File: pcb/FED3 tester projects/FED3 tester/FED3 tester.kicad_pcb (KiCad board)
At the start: 4 copper layers, 108 x 82 mm, 156 parts, among them J1 USB4105-GF-A, J2 6pin_hd, J3 Conn_02x03_Odd_Even, J4 MotorCkeck, J5 Motor, J6 Conn_02x03_Odd_Even, J7 Conn_01x02_Socket, K1 1462042-8, K2 1462042-8, K3 1462042-8, Q1 DMN63D8L-7, Q2 DMN63D8L-7, Q3 DMN63D8L-7, Q4 DMN63D8L-7, SW1 SW_SPST, SW2 SW_SPST, SW3 SW_SPST, SW4 SW_SPST, SW5 SW_SPST, U1 FT232RL, U2 LP5907MFX-3.3, U3 TPS79301-EP, U4 THS4281, U5 THS4281, U6 THS4281, U7 THS4281, U8 ZXCT1082, U9 ATXMEGA32A4U-MH

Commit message: FED3 Tester - 1º routing finalizado
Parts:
- removed C36: 100nF, Capacitor_SMD:C_0402_1005Metric_Pad0.74x0.62mm_HandSolder
- removed the SW4 at (174.8, 111.0)
- removed the SW4 at (185.4, 111.3)
- added L2: 40R@100MHz, Resistor_SMD:R_0805_2012Metric, F.Cu at (133.8, 101.6)
- C1, C14, C15, C16, C17, C18, C19, C2, C20, C21, C22, C23, C24, C25, C26, C27, C28, C29, C3, C30, C31, C32, C33, C34, C35: footprint Capacitor_SMD:C_0402_1005Metric_Pad0.74x0.62mm_HandSolder -> Capacitor_SMD:C_0402_1005Metric
- R26, R27: footprint Resistor_SMD:R_0603_1608Metric -> Resistor_SMD:R_0402_1005Metric
- TP12, TP2, TP5, TP6, TP7, TP8: footprint FED3_PCBLib:Pin_D1.70mm -> FED3_PCBLib:Pin_D1.75mm
- moved R30 23.7 mm to (200.5, 55.4), turned to 0 degrees
- moved C17 15.5 mm to (174.0, 68.9), turned to 180 degrees
- moved R12 13.4 mm to (174.0, 70.5), turned to 0 degrees
- moved R26 12.6 mm to (186.0, 79.4)
- moved R44 12.0 mm to (145.2, 97.4), turned to -90 degrees
- moved C1 11.9 mm to (108.8, 86.5), turned to 180 degrees
- moved R29 11.6 mm to (157.6, 75.8), turned to 90 degrees
- moved D8 11.4 mm to (145.1, 90.8), turned to 90 degrees
- moved C16 11.0 mm to (174.0, 72.2), turned to 0 degrees
- moved C3 10.6 mm to (113.8, 95.6), turned to 0 degrees
- moved R28 10.5 mm to (159.5, 75.7), turned to -90 degrees
- moved R25 10.1 mm to (184.1, 80.5), turned to -90 degrees
- moved R27 10.1 mm to (186.0, 81.7), turned to 180 degrees
- moved R2 9.67 mm to (116.6, 95.6), turned to 0 degrees
- moved C14 9.36 mm to (170.7, 75.4), turned to 90 degrees
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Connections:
- D1 pad 1: USB+5V -> RELAY+5V
- D10 pad 1: USB+5V -> RELAY+5V
- D8 pad 1: USB+5V -> RELAY+5V
- K1 pad 8: USB+5V -> RELAY+5V
- K2 pad 8: USB+5V -> RELAY+5V
- K3 pad 8: USB+5V -> RELAY+5V
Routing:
- net +3V3: track 10.9 -> 539.8 mm, vias 0 -> 25
- net RELAY+5V: track 0.00 -> 144.0 mm, vias 0 -> 6
- net /main core/FTDI_CTS: track 0.00 -> 93.3 mm, vias 0 -> 3
- net Net-(R50-Pad2): track 0.00 -> 91.0 mm, vias 0 -> 2
- net /main core/FTDI_RXD: track 0.00 -> 89.9 mm, vias 0 -> 3
- net USB+5V: track 25.8 -> 115.0 mm, vias 0 -> 3
- net /main core/FTDI_RTS: track 0.00 -> 88.8 mm, vias 0 -> 3
- net /main core/FTDI_TXD: track 0.00 -> 86.3 mm, vias 0 -> 3
- net /main core/ADC Bat_I: track 0.00 -> 72.7 mm, vias 0 -> 2
- net /main core/LED_CHRG: track 0.00 -> 66.8 mm, vias 0 -> 1
- net Net-(R35-Pad2): track 0.00 -> 62.8 mm, vias 0 -> 2
- net /main core/STATE_LED: track 0.00 -> 62.0 mm, vias 0 -> 3
- net /main core/VUSB_check: track 1.90 -> 62.0 mm, vias 0 -> 3
- net Net-(R49-Pad2): track 0.00 -> 54.8 mm, vias 0 -> 1
- net /main core/Relay_ThermalPin: track 2.07 -> 56.3 mm, vias 0 -> 2
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- added copper zone on F.Cu, net +3V3

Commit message: FED3-tester
- 'final' - antes de revisão com o Filipe
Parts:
- removed R31, R32, R33, R34, R35: 100R, Resistor_SMD:R_0402_1005Metric
- C10: value 15pF -> 150pF
- J4: value MotorCkeck -> MotorCkeck1
- J5: value Motor -> MotorCkeck2
- K1, K2, K3: value 1462042-8 -> Relay SPDT
- R7: value 60k8 -> 61k2
- moved G*** 19.1 mm to (132.2, 41.3)
- moved K1 4.12 mm to (164.3, 90.1)
- moved D1 3.83 mm to (164.3, 82.7)
- moved D10 1.85 mm to (187.1, 61.5)
- moved K3 1.85 mm to (195.6, 61.4)
- moved R30 1.85 mm to (198.7, 55.4)
- moved C29 1.40 mm to (155.9, 60.2)
- moved Q4 1.20 mm to (189.8, 68.5)
- moved R47 1.20 mm to (186.1, 67.6)
- moved R48 1.20 mm to (186.1, 69.5)
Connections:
- SW1 pad 2: Net-(R31-Pad2) -> /main core/START_SW
- SW2 pad 2: Net-(R32-Pad2) -> /main core/Buzzer_OK
- SW3 pad 2: Net-(R33-Pad2) -> /main core/Buzzer_NOK
- SW4 pad 2: Net-(R34-Pad2) -> /main core/Motor_OK
- SW5 pad 2: Net-(R35-Pad2) -> /main core/Motor_NOK
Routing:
- net /main core/Motor_NOK: track 5.17 -> 68.7 mm, vias 0 -> 2
- net Net-(R35-Pad2): track 62.8 -> 0.00 mm, vias 2 -> 0
- net Net-(R34-Pad2): track 47.2 -> 0.00 mm, vias 2 -> 0
- net /main core/Motor_OK: track 5.71 -> 52.7 mm, vias 0 -> 2
- net /main core/Buzzer_NOK: track 8.28 -> 54.7 mm, vias 0 -> 2
- net Net-(R33-Pad2): track 45.6 -> 0.00 mm, vias 2 -> 0
- net /main core/START_SW: track 5.10 -> 44.8 mm, vias 0 -> 2
- net Net-(R31-Pad2): track 38.9 -> 0.00 mm, vias 2 -> 0
- net /main core/Buzzer_OK: track 6.86 -> 45.5 mm, vias 0 -> 2
- net Net-(R32-Pad2): track 37.6 -> 0.00 mm, vias 2 -> 0
- net GND: track 61.1 -> 94.0 mm, vias 38 -> 71
- net RELAY+5V: track 144.0 -> 136.8 mm
- net Net-(K1-Pad3): track 33.3 -> 37.3 mm
- net /main core/ADC Bat_I: track 72.7 -> 70.0 mm
- net Net-(R49-Pad2): track 54.8 -> 52.7 mm
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- added copper zone on B.Cu, net +3V3
- added copper zone on In1.Cu, net +3V3
- added copper zone on In2.Cu, net +3V3
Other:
- board text added: "LED CHRG"
- board text added: "POWER EN"
- board text added: "tester rev.A"
- board text removed: "FED3 tester rev.A"
- board text removed: "LED_CHRG"
- board text removed: "POWER_EN"

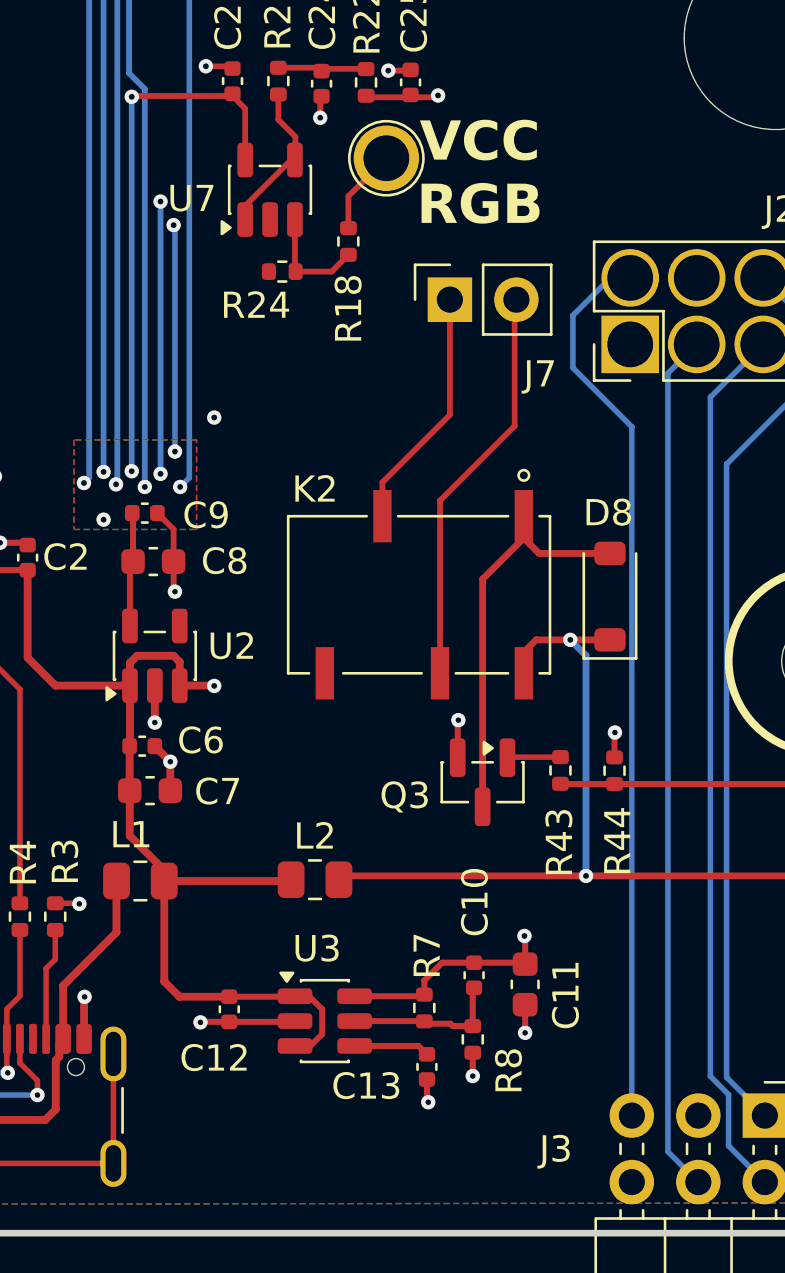
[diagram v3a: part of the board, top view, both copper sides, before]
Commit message: tunning com v.7.7
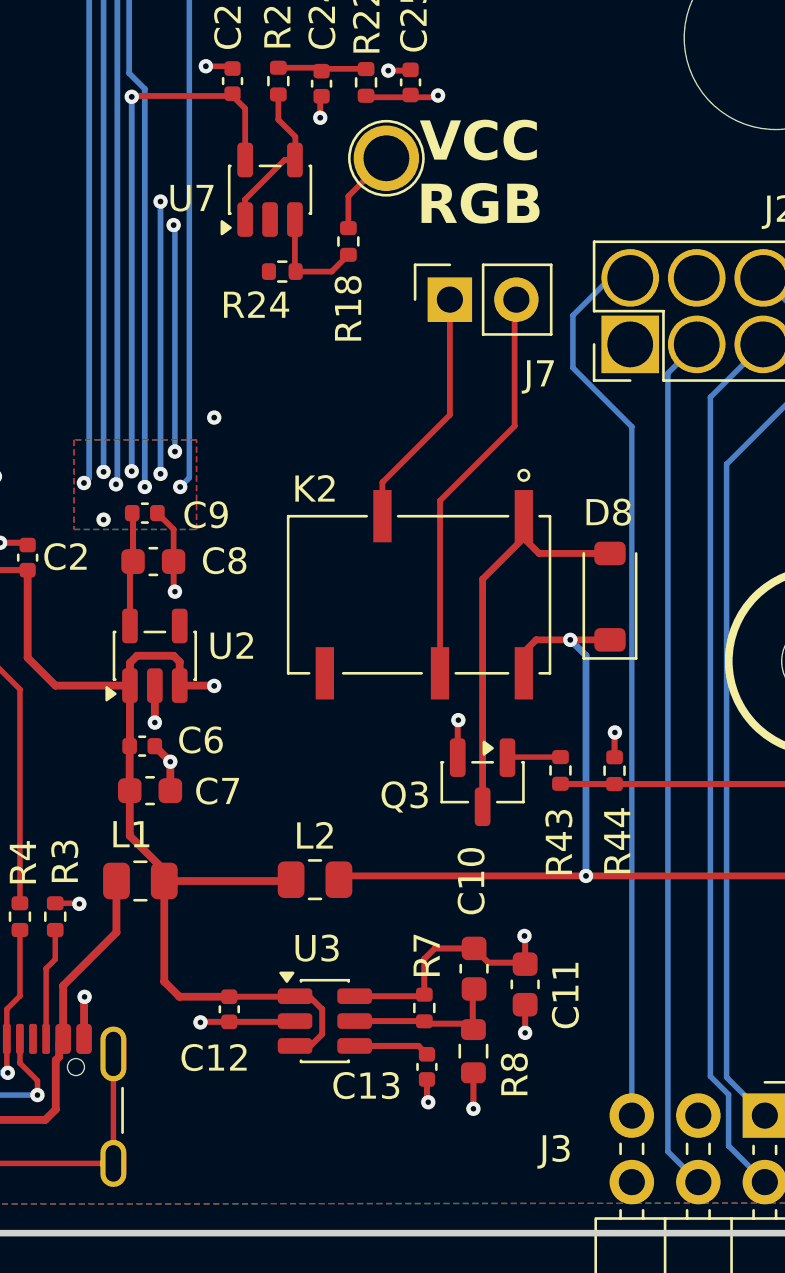
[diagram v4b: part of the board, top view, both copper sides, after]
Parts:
- C10: value 150pF -> 15pF; footprint Capacitor_SMD:C_0402_1005Metric -> Capacitor_SMD:C_0603_1608Metric
- R1, R15, R16, R23, R24, R3: value 5k1 -> 5.1k
- R26, R27: value 1k2 -> 1.2K
- R7: value 61k2 -> 61.2k
- R8: value 30k1 -> 30.1k; footprint Resistor_SMD:R_0402_1005Metric -> Resistor_SMD:R_0603_1608Metric
- U3: value TPS79301-EP -> TPS79301DBVRG4
- moved R8 0.45 mm to (139.8, 108.2)
- moved C10 0.25 mm to (139.9, 105.0)
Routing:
- net 3.7V: track 47.3 -> 48.2 mm
- net GND: track 94.0 -> 94.7 mm

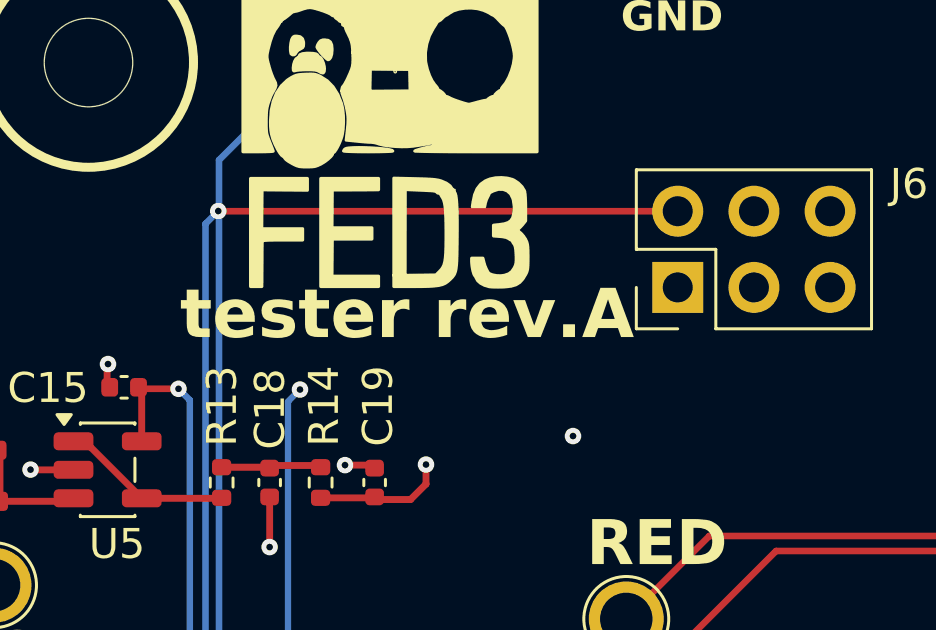
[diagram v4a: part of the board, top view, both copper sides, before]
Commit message: início FED3 tester - rev.B
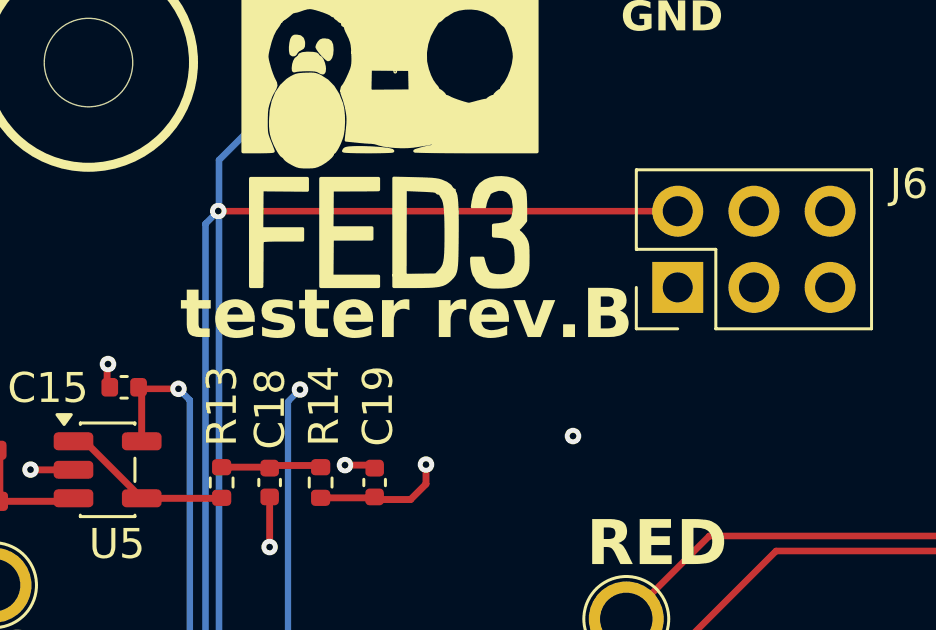
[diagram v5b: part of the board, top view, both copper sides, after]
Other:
- board text added: "tester rev.B"
- board text removed: "tester rev.A"
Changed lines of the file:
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@@
 		)
 	)
-	(gr_text "tester rev.A"
+	(gr_text "tester rev.B"
 		(at 125.4 49.8 0)
 		(layer "F.SilkS")

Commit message: FED3 tester project
.commit para sincronia
.ainda longe do final
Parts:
- removed the C20 at (112.2, 65.7)
- removed the C27 at (162.3, 50.7)
- removed the R19 at (115.0, 69.1)
- removed the R20 at (118.3, 69.1)
- removed the R23 at (107.1, 69.8)
- removed R49: 1k, Resistor_SMD:R_0402_1005Metric
- removed the TP11 at (120.0, 60.8)
- removed the U6 at (111.5, 68.6)
- added ?: , , F.Cu at (154.3, 183.4)
- added ?: , , F.Cu at (67.3, 183.5)
- added C10: 100nF, Capacitor_SMD:C_0402_1005Metric, F.Cu at (180.2, 17.0)
- added C11: 2.2uF, Capacitor_SMD:C_0603_1608Metric, F.Cu at (176.7, 17.3)
- added C12: 4.7uF, Capacitor_SMD:C_0603_1608Metric, F.Cu at (176.7, 19.8)
- added C13: 100nF, Capacitor_SMD:C_0402_1005Metric, F.Cu at (180.2, 19.0)
- added C24: 100nF, Capacitor_SMD:C_0402_1005Metric, F.Cu at (128.0, 143.7)
- added C25: 100nF, Capacitor_SMD:C_0402_1005Metric, F.Cu at (149.7, 144.4)
- added D5: Green, LED_SMD:LED_0603_1608Metric, F.Cu at (141.9, 116.8)
- added D8: Green, LED_SMD:LED_0603_1608Metric, F.Cu at (134.1, 182.9)
- added D9: Red, LED_SMD:LED_0603_1608Metric, F.Cu at (144.1, 182.8)
- added Q2: ???????, Package_TO_SOT_SMD:SOT-23, F.Cu at (75.6, 62.5)
- added Q3: DMN63D8L-7, Package_TO_SOT_SMD:SOT-23, F.Cu at (71.2, 62.5)
- added R13: 2k, Resistor_SMD:R_0402_1005Metric, F.Cu at (137.7, 116.8)
- added R18: 10k, Resistor_SMD:R_0402_1005Metric, F.Cu at (143.8, 176.7)
- added R27: 1.2K, Resistor_SMD:R_0402_1005Metric, F.Cu at (71.9, 58.6)
- added R29: 1.2K, Resistor_SMD:R_0402_1005Metric, F.Cu at (73.9, 58.6)
- added R32: 1.2K, Resistor_SMD:R_0402_1005Metric, F.Cu at (70.0, 58.6)
- added SW2: SW_SPST, Button_Switch_SMD:SW_SPST_TL3305B, F.Cu at (133.7, 101.2)
- added SW3: SW_SPST, Button_Switch_SMD:SW_SPST_TL3305B, F.Cu at (143.6, 101.2)
- added SW4: SW_SPST, Button_Switch_SMD:SW_SPST_TL3305B, F.Cu at (133.7, 144.8)
- added SW5: SW_SPST, Button_Switch_SMD:SW_SPST_TL3305B, F.Cu at (143.6, 144.8)
- added U3: LP5907MFX-3.3, Package_TO_SOT_SMD:SOT-23-5, F.Cu at (177.3, 13.8)
- C22, C23: value 15nF -> 100nF
- D1: renamed from D7; value Green LED -> Green
- D2: renamed from D6; value Green LED -> Green
- D3: renamed from D5; value Green LED -> Green
- D4: value Green LED -> Green
- D7: renamed from D3; value Green LED -> Red
- R10: renamed from R41; value 330R -> 2k
- R11: renamed from R40; value 330R -> 2k
- R12: renamed from R39; value 330R -> 2k
- R15: renamed from R38; value 330R -> 10k
- R17: value 10k -> 2k
- R9: renamed from R42; value 560R -> 2k
- moved R17 111.4 mm to (134.4, 176.3)
- moved C29 103.9 mm to (128.4, 162.4)
- moved C30 98.6 mm to (149.6, 162.5)
- moved J1 83.5 mm to (81.5, 184.5)
- moved J4 81.5 mm to (110.7, 181.4)
- moved SW9 78.5 mm to (143.6, 163.4)
- moved SW8 77.7 mm to (133.7, 163.4)
- moved C27 75.5 mm to (127.8, 125.1), turned to -90 degrees
- moved C28 67.2 mm to (150.2, 125.8), turned to -90 degrees
- moved SW7 47.7 mm to (143.6, 126.1)
- moved SW6 46.6 mm to (133.7, 126.1)
- moved C23 43.5 mm to (150.6, 100.0), turned to -90 degrees
- moved SW1 42.1 mm to (139.1, 80.5)
- moved ? 41.2 mm to (111.1, 60.6)
- moved C38 41.2 mm to (93.8, 62.3)
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- renumbered C10 to C14, C11 to C15, C12 to C16, C13 to C17, C26 to C18, C28 to C19, C29 to C20, C30 to C21, C35 to C26, C33 to C27, C34 to C28, C31 to C29, C32 to C30, C14 to C31, C15 to C32, C16 to C33, C17 to C34, C18 to C35, C19 to C36, C21 to C37, C24 to C38, C25 to C39, D1 to D10, D8 to D11, D10 to D12, D2 to D6, J6 to J2, J2 to J3, J3 to J4, J4 to J5, J5 to J6, Q2 to Q1, Q1 to Q4, Q3 to Q5, Q4 to Q6, R36 to R14, R37 to R16, R9 to R19, R10 to R20, R11 to R21, R12 to R22, R13 to R23, R14 to R24, R15 to R25, R16 to R26, R18 to R28, R21 to R30, R22 to R31, R24 to R33, R25 to R34, R50 to R35, R45 to R36, R26 to R37, R27 to R38, R28 to R39, R43 to R40, R29 to R41, R44 to R42, R46 to R43, R30 to R44, R47 to R45, R48 to R46, SW4 to SW6, SW5 to SW7, SW2 to SW8, SW3 to SW9, TP12 to TP11, TP13 to TP12, TP7 to TP4, TP8 to TP5, TP5 to TP6, TP6 to TP7, TP4 to TP8, U3 to U4, U9 to U5, U4 to U6, U5 to U7, U7 to U8, U8 to U9
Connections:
- net /main core/DUT stage/SWCLK renamed /main core/DUT stage/DUT_SWCLK
- net /main core/DUT stage/SWDIO renamed /main core/DUT stage/DUT_SWDIO
- net /main core/DUT stage/~{RESET} renamed /main core/DUT stage/DUT_~{RESET}
- C22 pad 1: Net-(C22-Pad1) -> /main core/Prog_OK
- C23 pad 1: /main core/VUSB_check -> /main core/Prog_NOK
- R10 pad 2: /main core/LED#3 -> /main core/LED#2
- R11 pad 2: /main core/LED#2 -> /main core/LED#3
- R12 pad 2: /main core/LED#1 -> /main core/LED#4
- R17 pad 2: /main core/DUT stage/VUSBtest -> /main core/PASS
- R9 pad 2: /main core/LED#4 -> /main core/LED#1
- TP8 pad 1: /main core/DUT stage/VUSBtest -> /main core/DUT stage/VUSB_out
- U5 pad 14: unconnected-(U9-PC4/OC1A/~{SS}-Pad14) -> /main core/LED#5
- U5 pad 15: unconnected-(U9-PC5/OC1B/MOSI/XCK1-Pad15) -> /main core/PASS
- U5 pad 16: unconnected-(U9-PC6/MISO/RXD1-Pad16) -> /main core/FAIL
- U5 pad 21: /main core/Buzzer_OK -> /main core/Prog_OK
- U5 pad 22: /main core/Buzzer_NOK -> /main core/Prog_NOK
- U5 pad 23: /main core/Motor_OK -> /main core/RGBW_OK
- U5 pad 24: /main core/Motor_NOK -> /main core/RGBW_NOK
- U5 pad 25: unconnected-(U9-PD5/OC1B/XCK1/MOSI-Pad25) -> /main core/Motor_OK
- U5 pad 26: /main core/~{RESET}_Test -> /main core/Motor_NOK
- U5 pad 27: /main core/POWER_EN -> /main core/Buzzer_OK
- U5 pad 39: +3V3 -> AVCC
- U5 pad 40: /main core/VBattest_check -> /main core/Buzzer_NOK
- U5 pad 41: /main core/VUSB_check -> /main core/VBattest_check
- U5 pad 42: /main core/VccRGB_check -> /main core/VUSB_2DUT
- U5 pad 6: unconnected-(U9-PB2/ADC10/DAC0-Pad6) -> /main core/I ON/OFF Test
- U5 pad 7: /main core/I ON/OFF Test -> /main core/POWER_EN
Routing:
- net /main core/Motor_NOK: track 68.7 -> 4.18 mm, vias 2 -> 0
- net /main core/VUSB_check: track 61.7 -> 0.00 mm, vias 3 -> 0
- net /main core/VBattest_check: track 34.8 -> 93.7 mm, vias 3 -> 5
- net /main core/Buzzer_NOK: track 54.7 -> 0.00 mm, vias 2 -> 0
- net /main core/Motor_OK: track 52.7 -> 0.00 mm, vias 2 -> 0
- net Net-(R49-Pad2): track 52.7 -> 0.00 mm, vias 1 -> 0
- net (no net): track 0.00 -> 52.7 mm, vias 0 -> 1
- net /main core/Buzzer_OK: track 45.5 -> 0.00 mm, vias 2 -> 0
- net /main core/Prog_NOK: track 0.00 -> 37.9 mm, vias 0 -> 2
- net /main core/Prog_OK: track 0.00 -> 36.3 mm, vias 0 -> 2
- net GND: track 94.7 -> 70.5 mm, vias 71 -> 55
- net /main core/RGBW_NOK: track 0.00 -> 19.8 mm, vias 0 -> 1
- net RELAY+5V: track 136.8 -> 118.4 mm
- net /main core/RGBW_OK: track 0.00 -> 16.1 mm, vias 0 -> 1
- net Net-(U6--) (its old number): track 4.97 -> 0.00 mm
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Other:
- board size 108 x 82 mm -> 108 x 164 mm
- board text added: "FINAL RESULT"
- board text added: "all rgbw ok?"
- board text added: "buzzer ok?"
- board text added: "motor moved left & right?"
- board text added: "programming ok?"
- board text removed: "STEP 1"
- board text removed: "STEP 2"

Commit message: FED3 tester - sync of the week
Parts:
- removed C14: 15pF, Capacitor_SMD:C_0603_1608Metric
- removed the C17 at (97.8, 99.9)
- added R39: 640k, Resistor_SMD:R_0402_1005Metric, F.Cu at (60.7, 39.3)
- added R42: 1M, Resistor_SMD:R_0402_1005Metric, F.Cu at (60.7, 41.3)
- C15: value 4.7uF -> 10uF; footprint Capacitor_SMD:C_0603_1608Metric -> Capacitor_SMD:C_1206_3216Metric
- R29: value 1.2K -> 1.2K ??
- R7: value 61.2k -> 8k2
- R8: value 30.1k -> 4k; footprint Resistor_SMD:R_0603_1608Metric -> Resistor_SMD:R_0402_1005Metric
- U4: value TPS79301DBVRG4 -> TPS73801DCQR; footprint Package_TO_SOT_SMD:SOT-23-6 -> Package_TO_SOT_SMD:SOT-223-6
- moved D7 62.3 mm to (54.3, 86.6), turned to -90 degrees
- moved C2 62.0 mm to (85.2, 142.4), turned to 0 degrees
- moved R15 59.0 mm to (56.8, 86.9)
- moved U1 56.4 mm to (85.7, 135.4), turned to -90 degrees
- moved C1 54.4 mm to (88.0, 128.4), turned to 90 degrees
- moved C5 52.5 mm to (76.4, 147.5)
- moved R1 52.5 mm to (79.6, 146.6)
- moved R3 52.5 mm to (83.6, 146.6)
- moved R4 52.5 mm to (82.3, 146.6)
- moved R5 52.5 mm to (80.9, 146.6)
- moved C4 52.5 mm to (76.4, 149.0)
- moved R6 52.5 mm to (76.4, 146.2)
- moved R2 49.5 mm to (78.9, 136.2), turned to -90 degrees
- moved C3 47.0 mm to (78.9, 133.4), turned to -90 degrees
- moved L1 44.3 mm to (74.3, 135.3), turned to 90 degrees
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- renumbered C18 to C17, C19 to C18, C20 to C19, C21 to C20, C22 to C21, C23 to C22, C24 to C23, C25 to C24, C26 to C25, C27 to C26, C28 to C27, C29 to C28, C30 to C29, C31 to C30, C32 to C31, C33 to C32, C34 to C33, C35 to C34, C36 to C35, C37 to C36, C38 to C37, C39 to C38, R39 to R40, R40 to R41, R41 to R43, R42 to R44, R43 to R45, R44 to R46, R45 to R47, R46 to R48
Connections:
- TP10 pad 1: /main core/LED_CHRG -> Net-(R39-Pad2)
- U4 pad 2: GND -> 3.7V
- U4 pad 3: USB+5V -> GND
- U4 pad 4: Net-(U4-BP) -> Net-(U4-FB)
- U4 pad 5: Net-(U4-FB) -> USB+5V
- U4 pad 6: 3.7V -> GND
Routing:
- net /main core/DUT stage/DUT_~{RESET}: track 33.5 -> 85.1 mm
- net /main core/DUT stage/DUT_SWCLK: track 33.7 -> 85.1 mm
- net +3V3: track 537.7 -> 487.0 mm
- net /main core/DUT stage/DUT_SWDIO: track 32.9 -> 83.0 mm
- net /main core/FTDI_CTS: track 93.6 -> 136.3 mm
- net /main core/FTDI_RXD: track 90.2 -> 131.7 mm
- net /main core/FTDI_TXD: track 86.6 -> 125.1 mm
- net /main core/FTDI_RTS: track 89.2 -> 126.9 mm
- net 3.7V: track 48.2 -> 13.5 mm, vias 3 -> 2
- net RELAY+5V: track 118.4 -> 84.3 mm
- net USB+5V: track 113.6 -> 90.3 mm
- net /USBD-: track 12.2 -> 0.00 mm
- net /USBD+: track 9.93 -> 0.00 mm
- net /main core/STATE_LED: track 60.9 -> 51.6 mm
- net GND: track 70.5 -> 63.5 mm, vias 55 -> 47
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- removed copper zone on B.Cu, net GND
- removed copper zone on F.Cu, net GND
- removed copper zone on In1.Cu, net GND
- removed copper zone on In2.Cu, net GND
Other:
- board size 108 x 164 mm -> 108 x 134.4 mm
- board text added: "3V3 & VBAT"
- board text added: "All RGB show B, G, R, and W?"
- board text added: "Buzzer ok?"
- board text added: "CURRENT"
- board text added: "LEDS"
- board text added: "Motor moved left and right?"
- board text added: "Programming ok?"
- board text added: "READY 2PROGRAM"
- board text removed: "all rgbw ok?"
- board text removed: "buzzer ok?"
- board text removed: "motor moved left & right?"
- board text removed: "programming ok?"
